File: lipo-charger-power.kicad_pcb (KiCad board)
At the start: 2 copper layers, 32 x 22 mm, 24 parts, among them J1 USB-MICROB, J2 BAT, J3 SENSE, J4 VREG, U1 TP4056, U2 NCP1529

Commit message: small size changes
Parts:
- J3: footprint HEADER-1x2:HEADER-1x2 -> kicad-libs:HEADER-1x2
- MH1, MH2, MH3, MH4: footprint kicad-libs:HOLE-M2-COND -> kicad-libs:HOLE-M2.5-COND

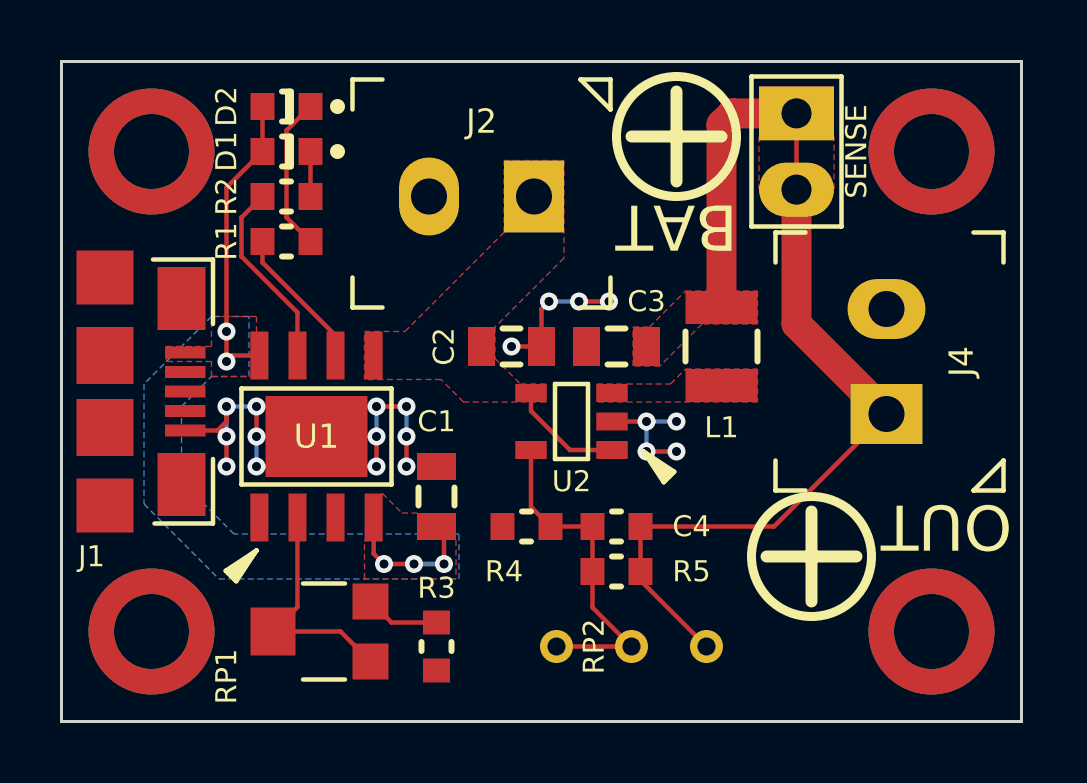
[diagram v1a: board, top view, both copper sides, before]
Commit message: add part numbers
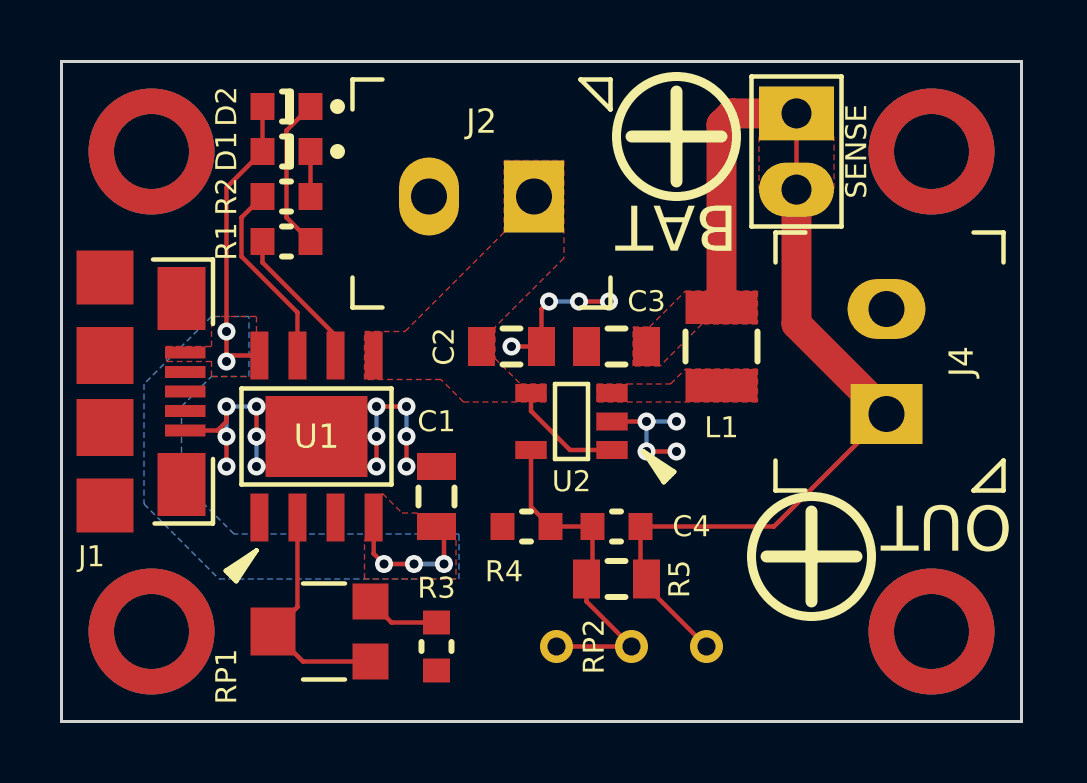
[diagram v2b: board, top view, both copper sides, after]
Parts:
- R5: footprint SMD-1608:SMD-1608 -> SMD-2012:SMD-2012
- moved R5 0.25 mm to (136.5, 104.2)
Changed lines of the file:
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@@
     (links 50)
     (no_connects 0)
-    (area 117.949999 86.949999 150.050001 109.050001)
+    (area 114.27262 86.285 151.653572 109.225001)
     (thickness 1.6)
     (drawings 14)
-    (tracks 102)
+    (tracks 105)
     (zones 0)
     (modules 24)
@@
       (drillshape 0)
       (scaleselection 1)
-      (outputdirectory ""))
+      (outputdirectory fab/))
   )
   (net 0 "")
@@
       (net 2 PGND))
   )
-  (module SMD-1608:SMD-1608 (layer F.Cu)
-    (at 136.5 104 270)
-    (fp_text reference R5 (at 0 -2.5 360) (layer F.SilkS)
-      (effects (font (size 0.7 0.7) (thickness 0.15)))
-    )
-    (fp_text value "1.15M 1%" (at 1.35 0 360) (layer F.SilkS) hide
-      (effects (font (size 0.7 0.7) (thickness 0.15)))
-    )
-    (fp_line (start 0.75 1.5) (end 0.75 -1.5) (layer Cmts.User) (width 0.05))
-    (fp_line (start 0.75 -1.5) (end -0.75 -1.5) (layer Cmts.User) (width 0.05))
-    (fp_line (start -0.75 -1.5) (end -0.75 1.5) (layer Cmts.User) (width 0.05))
-    (fp_line (start -0.75 1.5) (end 0.75 1.5) (layer Cmts.User) (width 0.05))
-    (fp_line (start -0.5 -0.15) (end -0.5 0.15) (layer F.SilkS) (width 0.2))
-    (fp_line (start 0.5 -0.15) (end 0.5 0.15) (layer F.SilkS) (width 0.2))
-    (pad 1 smd rect (at 0 -0.8 270) (size 0.9 0.8) (layers F.Cu F.Paste F.Mask)
-      (net 4 /VREG))
-    (pad 2 smd rect (at 0 0.8 270) (size 0.9 0.8) (layers F.Cu F.Paste F.Mask)
-      (net 13 "Net-(C4-Pad1)"))
-  )
   (module kicad-libs:SMD-POT-3831 (layer F.Cu)
     (at 126.5 106 90)
@@
     (pad 1 thru_hole circle (at 0 0) (size 2.5 2.5) (drill 2.5) (layers *.Cu)
       (net 10 "Net-(MH4-Pad1)") (clearance 0.2) (zone_connect 2))
+  )
+  (module SMD-2012:SMD-2012 (layer F.Cu)
+    (at 136.5 104.25 270)
+    (fp_text reference R5 (at 0 -2.1 270) (layer F.SilkS)
+      (effects (font (size 0.7 0.7) (thickness 0.15)))
+    )
+    (fp_text value "1.15M 1%" (at 1.525 0 360) (layer F.SilkS) hide
+      (effects (font (size 0.7 0.7) (thickness 0.15)))
+    )
+    (fp_line (start -0.6 0.3) (end -0.6 -0.3) (layer F.SilkS) (width 0.2))
+    (fp_line (start 0.6 -0.3) (end 0.6 0.3) (layer F.SilkS) (width 0.2))
+    (fp_line (start 0.9 -1.7) (end 0.9 1.7) (layer Cmts.User) (width 0.05))
+    (fp_line (start 0.9 1.7) (end -0.9 1.7) (layer Cmts.User) (width 0.05))
+    (fp_line (start -0.9 1.7) (end -0.9 -1.7) (layer Cmts.User) (width 0.05))
+    (fp_line (start -0.9 -1.7) (end 0.9 -1.7) (layer Cmts.User) (width 0.05))
+    (pad 1 smd rect (at 0 -1 270) (size 1.3 0.9) (layers F.Cu F.Paste F.Mask)
+      (net 4 /VREG))
+    (pad 2 smd rect (at 0 1 270) (size 1.3 0.9) (layers F.Cu F.Paste F.Mask)
+      (net 13 "Net-(C4-Pad1)"))
   )
   (gr_text ")satellite(" (at 138 104.25) (layer B.Mask)
@@
   (segment (start 142.5 95.75) (end 145.5 98.75) (width 1) (layer F.Cu) (net 4))
   (segment (start 142.5 91.27) (end 142.5 95.75) (width 1) (layer F.Cu) (net 4))
-  (segment (start 137.3 104.3) (end 139.5 106.5) (width 0.15) (layer F.Cu) (net 4))
   (segment (start 137.3 104) (end 137.3 104.3) (width 0.15) (layer F.Cu) (net 4))
-  (segment (start 137.3 104) (end 137.3 102.5) (width 0.15) (layer F.Cu) (net 4))
   (segment (start 141.75 102.5) (end 137.3 102.5) (width 0.15) (layer F.Cu) (net 4))
   (segment (start 145.5 98.75) (end 141.75 102.5) (width 0.15) (layer F.Cu) (net 4))
   (segment (start 142.5 88.73) (end 142.5 91.27) (width 0.15) (layer F.Cu) (net 4))
+  (segment (start 137.3 104.05) (end 137.5 104.25) (width 0.15) (layer F.Cu) (net 4))
+  (segment (start 137.3 102.5) (end 137.3 104.05) (width 0.15) (layer F.Cu) (net 4))
+  (segment (start 137.5 104.5) (end 139.5 106.5) (width 0.15) (layer F.Cu) (net 4))
+  (segment (start 137.5 104.25) (end 137.5 104.5) (width 0.15) (layer F.Cu) (net 4))
   (segment (start 126.3 91.5) (end 126.3 90) (width 0.15) (layer F.Cu) (net 5))
   (segment (start 125.5 92.2) (end 125.5 89.3) (width 0.15) (layer F.Cu) (net 6))
@@
   (segment (start 134.3 102.5) (end 133.65 101.85) (width 0.15) (layer F.Cu) (net 13))
   (segment (start 134.3 102.5) (end 135.7 102.5) (width 0.15) (layer F.Cu) (net 13))
-  (segment (start 135.7 102.5) (end 135.7 104) (width 0.15) (layer F.Cu) (net 13))
   (segment (start 134.5 106.5) (end 137 106.5) (width 0.15) (layer F.Cu) (net 13))
-  (segment (start 135.7 105.2) (end 137 106.5) (width 0.15) (layer F.Cu) (net 13))
-  (segment (start 135.7 104) (end 135.7 105.2) (width 0.15) (layer F.Cu) (net 13))
+  (segment (start 135.7 104.05) (end 135.5 104.25) (width 0.15) (layer F.Cu) (net 13))
+  (segment (start 135.7 102.5) (end 135.7 104.05) (width 0.15) (layer F.Cu) (net 13))
+  (segment (start 135.5 105) (end 137 106.5) (width 0.15) (layer F.Cu) (net 13))
+  (segment (start 135.5 104.25) (end 135.5 105) (width 0.15) (layer F.Cu) (net 13))
   (segment (start 125.865 105.185) (end 125.05 106) (width 0.15) (layer F.Cu) (net 14))
   (segment (start 125.865 102.2) (end 125.865 105.185) (width 0.15) (layer F.Cu) (net 14))
-  (segment (start 127.3 106) (end 128.3 107) (width 0.15) (layer F.Cu) (net 14))
-  (segment (start 125.05 106) (end 127.3 106) (width 0.15) (layer F.Cu) (net 14))
+  (segment (start 126.05 107) (end 128.3 107) (width 0.15) (layer F.Cu) (net 14))
+  (segment (start 125.05 106) (end 126.05 107) (width 0.15) (layer F.Cu) (net 14))
   (segment (start 124.7 93.7) (end 124.7 93) (width 0.15) (layer F.Cu) (net 15))
   (segment (start 127.135 96.135) (end 124.7 93.7) (width 0.15) (layer F.Cu) (net 15))

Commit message: update
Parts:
- C1, C2, C3, R5: footprint SMD-2012:SMD-2012 -> kicad-libs:SMD-2012
- C4, R1, R2, R3, R4: footprint SMD-1608:SMD-1608 -> kicad-libs:SMD-1608
- U2: footprint sot-23-5:SOT-23-5 -> kicad-libs:SOT-23-5
